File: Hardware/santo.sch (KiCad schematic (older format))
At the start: 7 parts

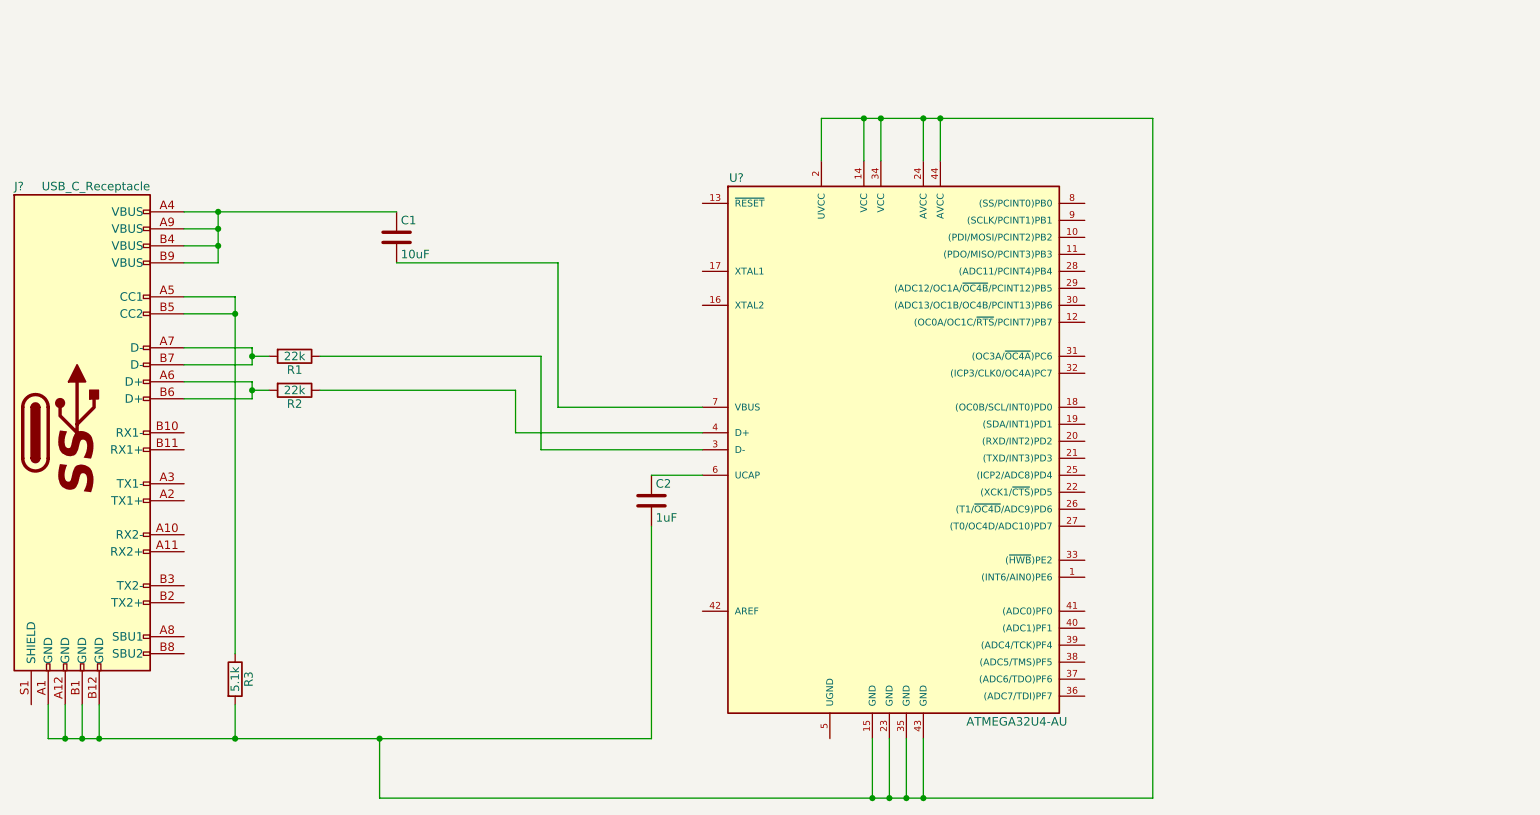
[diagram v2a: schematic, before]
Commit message: Fix title and center
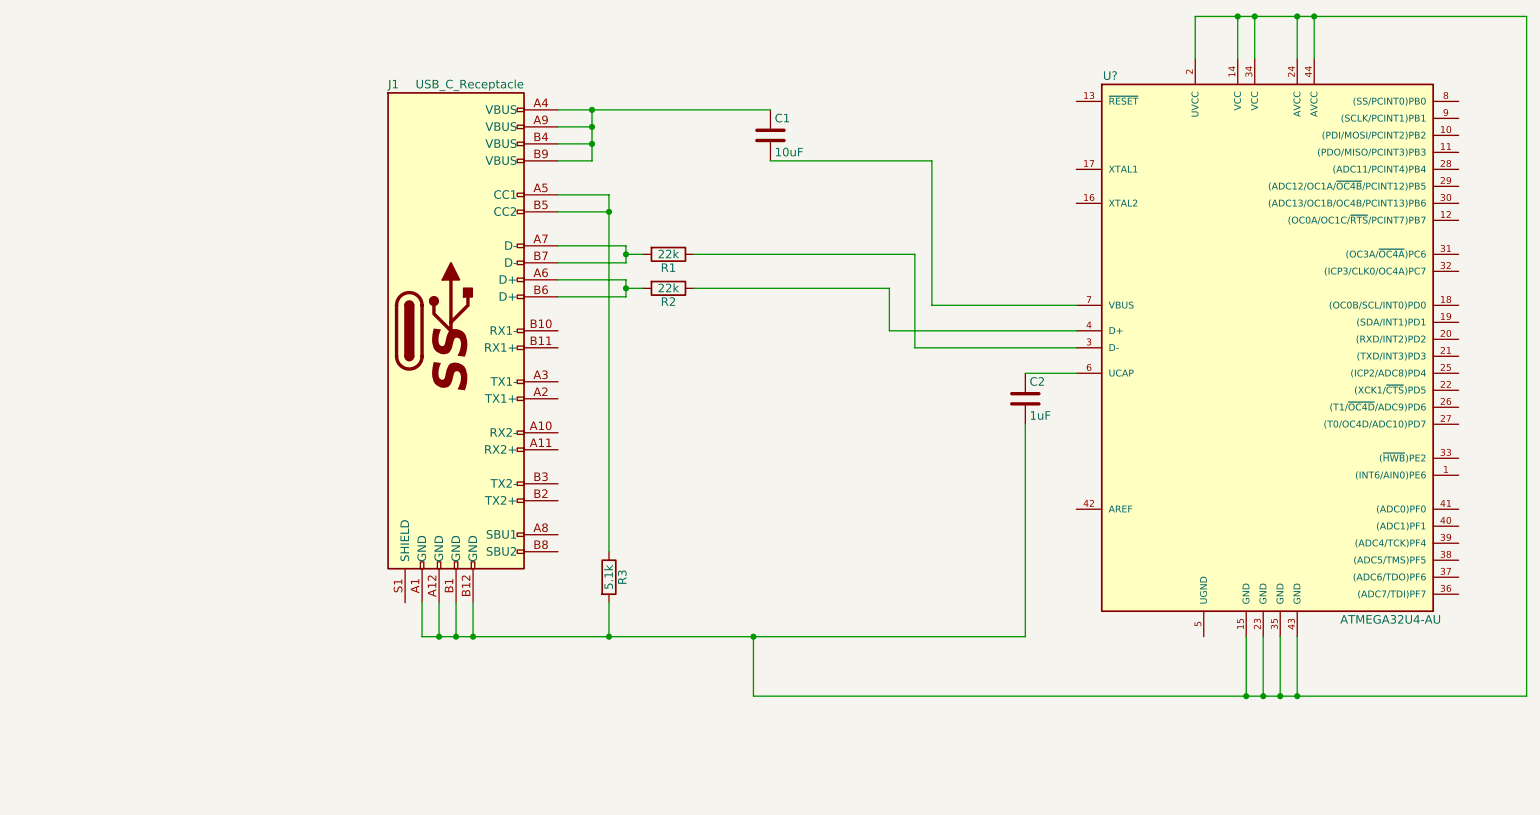
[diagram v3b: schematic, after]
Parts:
- gave numbers to parts that had none: 1
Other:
- moved on the sheet: C1, C2, J1, R1, R2, R3, U?
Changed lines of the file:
@@
 encoding utf-8
 Sheet 1 1
-Title "Controller and Board"
+Title "USB-C Receptacle to Microcontroller"
 Date "2017-10-27"
 Rev "0"
@@
 L ATMEGA32U4-AU U?
 U 1 1 59F3E9EC
-P 5800 4350
-F 0 "U?" H 4850 6050 50  0000 C CNN
-F 1 "ATMEGA32U4-AU" H 6500 2850 50  0000 C CNN
-F 2 "TQFP44" H 5800 4350 50  0001 C CIN
-F 3 "" H 6900 5450 50  0001 C CNN
-	1    5800 4350
-	1    0    0    -1
-$EndComp
-$Comp
-L USB_C_Receptacle J?
+P 8000 3750
+F 0 "U?" H 7050 5450 50  0000 C CNN
+F 1 "ATMEGA32U4-AU" H 8700 2250 50  0000 C CNN
+F 2 "TQFP44" H 8000 3750 50  0001 C CIN
+F 3 "" H 9100 4850 50  0001 C CNN
+	1    8000 3750
+	1    0    0    -1
+$EndComp
+$Comp
+L USB_C_Receptacle J1
 U 1 1 59F5288B
-P 1000 4150
-F 0 "J?" H 600 5600 50  0000 L CNN
-F 1 "USB_C_Receptacle" H 1400 5600 50  0000 R CNN
-F 2 "" H 1150 4150 50  0001 C CNN
-F 3 "" H 1150 4150 50  0001 C CNN
-	1    1000 4150
-	1    0    0    -1
-$EndComp
-Wire Wire Line
-	1600 2950 1800 2950
-Wire Wire Line
-	1800 2850 1800 3150
-Connection ~ 1800 2850
-Wire Wire Line
-	1800 3050 1600 3050
-Connection ~ 1800 2950
-Wire Wire Line
-	1800 3150 1600 3150
-Connection ~ 1800 3050
-Wire Wire Line
-	1600 2850 2850 2850
+P 3200 3550
+F 0 "J1" H 2800 5000 50  0000 L CNN
+F 1 "USB_C_Receptacle" H 3600 5000 50  0000 R CNN
+F 2 "" H 3350 3550 50  0001 C CNN
+F 3 "" H 3350 3550 50  0001 C CNN
+	1    3200 3550
+	1    0    0    -1
+$EndComp
+Wire Wire Line
+	3800 2350 4000 2350
+Wire Wire Line
+	4000 2250 4000 2550
+Connection ~ 4000 2250
+Wire Wire Line
+	4000 2450 3800 2450
+Connection ~ 4000 2350
+Wire Wire Line
+	4000 2550 3800 2550
+Connection ~ 4000 2450
+Wire Wire Line
+	3800 2250 5050 2250
 $Comp
 L C C1
 U 1 1 59F5311D
-P 2850 3000
-F 0 "C1" H 2875 3100 50  0000 L CNN
-F 1 "10uF" H 2875 2900 50  0000 L CNN
-F 2 "" H 2888 2850 50  0001 C CNN
-F 3 "" H 2850 3000 50  0001 C CNN
-	1    2850 3000
-	1    0    0    -1
-$EndComp
-Wire Wire Line
-	2850 3150 3800 3150
-Wire Wire Line
-	3800 3150 3800 4000
-Wire Wire Line
-	3800 4000 4650 4000
+P 5050 2400
+F 0 "C1" H 5075 2500 50  0000 L CNN
+F 1 "10uF" H 5075 2300 50  0000 L CNN
+F 2 "" H 5088 2250 50  0001 C CNN
+F 3 "" H 5050 2400 50  0001 C CNN
+	1    5050 2400
+	1    0    0    -1
+$EndComp
+Wire Wire Line
+	5050 2550 6000 2550
+Wire Wire Line
+	6000 2550 6000 3400
+Wire Wire Line
+	6000 3400 6850 3400
 $Comp
 L C C2
 U 1 1 59F532C4
-P 4350 4550
-F 0 "C2" H 4375 4650 50  0000 L CNN
-F 1 "1uF" H 4375 4450 50  0000 L CNN
-F 2 "" H 4388 4400 50  0001 C CNN
-F 3 "" H 4350 4550 50  0001 C CNN
-	1    4350 4550
-	1    0    0    -1
-$EndComp
-Wire Wire Line
-	4350 4400 4650 4400
-Wire Wire Line
-	4350 4700 4350 5950
-Wire Wire Line
-	4350 5950 800  5950
-Wire Wire Line
-	800  5950 800  5750
-Wire Wire Line
-	900  5750 900  5950
-Connection ~ 900  5950
-Wire Wire Line
-	1000 5750 1000 5950
-Connection ~ 1000 5950
-Wire Wire Line
-	1100 5750 1100 5950
-Connection ~ 1100 5950
-Wire Wire Line
-	5350 2550 5350 2300
-Wire Wire Line
-	5350 2300 7300 2300
-Wire Wire Line
-	7300 2300 7300 6300
-Wire Wire Line
-	7300 6300 2750 6300
-Wire Wire Line
-	2750 6300 2750 5950
-Connection ~ 2750 5950
-Wire Wire Line
-	5600 2550 5600 2300
-Connection ~ 5600 2300
-Wire Wire Line
-	5700 2550 5700 2300
-Connection ~ 5700 2300
-Wire Wire Line
-	5950 2550 5950 2300
-Connection ~ 5950 2300
-Wire Wire Line
-	6050 2550 6050 2300
-Connection ~ 6050 2300
-Wire Wire Line
-	5650 5950 5650 6300
-Connection ~ 5650 6300
-Wire Wire Line
-	5750 5950 5750 6300
-Connection ~ 5750 6300
-Wire Wire Line
-	5850 5950 5850 6300
-Connection ~ 5850 6300
-Wire Wire Line
-	5950 5950 5950 6300
-Connection ~ 5950 6300
+P 6550 3950
+F 0 "C2" H 6575 4050 50  0000 L CNN
+F 1 "1uF" H 6575 3850 50  0000 L CNN
+F 2 "" H 6588 3800 50  0001 C CNN
+F 3 "" H 6550 3950 50  0001 C CNN
+	1    6550 3950
+	1    0    0    -1
+$EndComp
+Wire Wire Line
+	6550 3800 6850 3800
+Wire Wire Line
+	6550 4100 6550 5350
+Wire Wire Line
+	6550 5350 3000 5350
+Wire Wire Line
+	3000 5350 3000 5150
+Wire Wire Line
+	3100 5150 3100 5350
+Connection ~ 3100 5350
+Wire Wire Line
+	3200 5150 3200 5350
+Connection ~ 3200 5350
+Wire Wire Line
+	3300 5150 3300 5350
+Connection ~ 3300 5350
+Wire Wire Line
+	7550 1950 7550 1700
+Wire Wire Line
+	7550 1700 9500 1700
+Wire Wire Line
+	9500 1700 9500 5700
+Wire Wire Line
+	9500 5700 4950 5700
+Wire Wire Line
+	4950 5700 4950 5350
+Connection ~ 4950 5350
+Wire Wire Line
+	7800 1950 7800 1700
+Connection ~ 7800 1700
+Wire Wire Line
+	7900 1950 7900 1700
+Connection ~ 7900 1700
+Wire Wire Line
+	8150 1950 8150 1700
+Connection ~ 8150 1700
+Wire Wire Line
+	8250 1950 8250 1700
+Connection ~ 8250 1700
+Wire Wire Line
+	7850 5350 7850 5700
+Connection ~ 7850 5700
+Wire Wire Line
+	7950 5350 7950 5700
+Connection ~ 7950 5700
+Wire Wire Line
+	8050 5350 8050 5700
+Connection ~ 8050 5700
+Wire Wire Line
+	8150 5350 8150 5700
+Connection ~ 8150 5700
 $Comp
 L R R3
 U 1 1 59F605C4
-P 1900 5600
-F 0 "R3" V 1980 5600 50  0000 C CNN
-F 1 "5.1k" V 1900 5600 50  0000 C CNN
-F 2 "" V 1830 5600 50  0001 C CNN
-F 3 "" H 1900 5600 50  0001 C CNN
-	1    1900 5600
-	1    0    0    -1
-$EndComp
-Wire Wire Line
-	1600 3350 1900 3350
-Wire Wire Line
-	1900 3350 1900 5450
-Wire Wire Line
-	1600 3450 1900 3450
-Connection ~ 1900 3450
-Wire Wire Line
-	1900 5750 1900 5950
-Connection ~ 1900 5950
+P 4100 5000
+F 0 "R3" V 4180 5000 50  0000 C CNN
+F 1 "5.1k" V 4100 5000 50  0000 C CNN
+F 2 "" V 4030 5000 50  0001 C CNN
+F 3 "" H 4100 5000 50  0001 C CNN
+	1    4100 5000
+	1    0    0    -1
+$EndComp
+Wire Wire Line
+	3800 2750 4100 2750
+Wire Wire Line
+	4100 2750 4100 4850
+Wire Wire Line
+	3800 2850 4100 2850
+Connection ~ 4100 2850
+Wire Wire Line
+	4100 5150 4100 5350
+Connection ~ 4100 5350
 $Comp
 L R R1
 U 1 1 59F60892
-P 2250 3700
-F 0 "R1" V 2330 3700 50  0000 C CNN
-F 1 "22k" V 2250 3700 50  0000 C CNN
-F 2 "" V 2180 3700 50  0001 C CNN
-F 3 "" H 2250 3700 50  0001 C CNN
-	1    2250 3700
+P 4450 3100
+F 0 "R1" V 4530 3100 50  0000 C CNN
+F 1 "22k" V 4450 3100 50  0000 C CNN
+F 2 "" V 4380 3100 50  0001 C CNN
+F 3 "" H 4450 3100 50  0001 C CNN
+	1    4450 3100
 	0    1    1    0
 $EndComp
@@
 L R R2
 U 1 1 59F608F2
-P 2250 3900
-F 0 "R2" V 2330 3900 50  0000 C CNN
-F 1 "22k" V 2250 3900 50  0000 C CNN
-F 2 "" V 2180 3900 50  0001 C CNN
-F 3 "" H 2250 3900 50  0001 C CNN
-	1    2250 3900
+P 4450 3300
+F 0 "R2" V 4530 3300 50  0000 C CNN
+F 1 "22k" V 4450 3300 50  0000 C CNN
+F 2 "" V 4380 3300 50  0001 C CNN
+F 3 "" H 4450 3300 50  0001 C CNN
+	1    4450 3300
 	0    1    1    0
 $EndComp
 Wire Wire Line
-	1600 3650 2000 3650
-Wire Wire Line
-	2000 3650 2000 3750
-Wire Wire Line
-	2000 3700 2100 3700
-Wire Wire Line
-	2000 3750 1600 3750
-Connection ~ 2000 3700
-Wire Wire Line
-	2000 3950 1600 3950
-Wire Wire Line
-	2000 3850 2000 3950
-Wire Wire Line
-	2000 3900 2100 3900
-Wire Wire Line
-	1600 3850 2000 3850
-Connection ~ 2000 3900
-Wire Wire Line
-	2400 3700 3700 3700
-Wire Wire Line
-	3700 3700 3700 4250
-Wire Wire Line
-	3700 4250 4650 4250
-Wire Wire Line
-	2400 3900 3550 3900
-Wire Wire Line
-	3550 3900 3550 4150
-Wire Wire Line
-	3550 4150 4650 4150
+	3800 3050 4200 3050
+Wire Wire Line
+	4200 3050 4200 3150
+Wire Wire Line
+	4200 3100 4300 3100
+Wire Wire Line
+	4200 3150 3800 3150
+Connection ~ 4200 3100
+Wire Wire Line
+	4200 3350 3800 3350
+Wire Wire Line
+	4200 3250 4200 3350
+Wire Wire Line
+	4200 3300 4300 3300
+Wire Wire Line
+	3800 3250 4200 3250
+Connection ~ 4200 3300
+Wire Wire Line
+	4600 3100 5900 3100
+Wire Wire Line
+	5900 3100 5900 3650
+Wire Wire Line
+	5900 3650 6850 3650
+Wire Wire Line
+	4600 3300 5750 3300
+Wire Wire Line
+	5750 3300 5750 3550
+Wire Wire Line
+	5750 3550 6850 3550
 $EndSCHEMATC

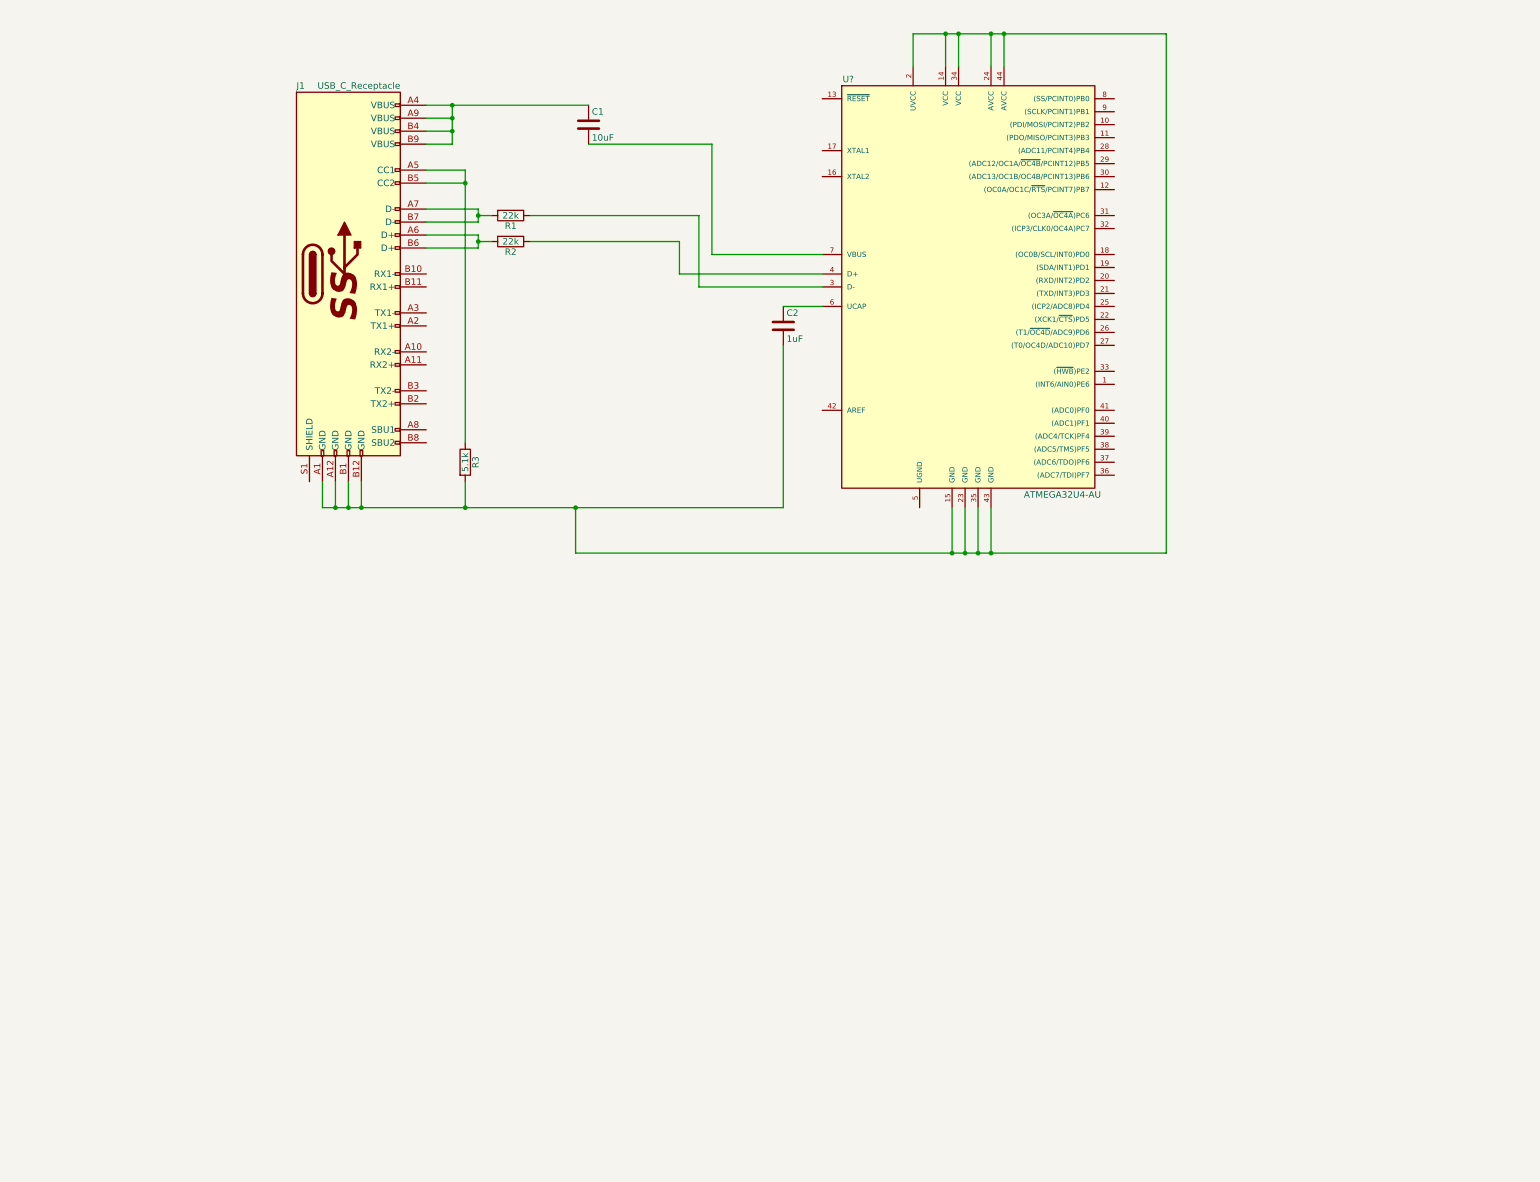
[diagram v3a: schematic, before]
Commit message: Fix the wiring for USB-C & Add TRRS Jack
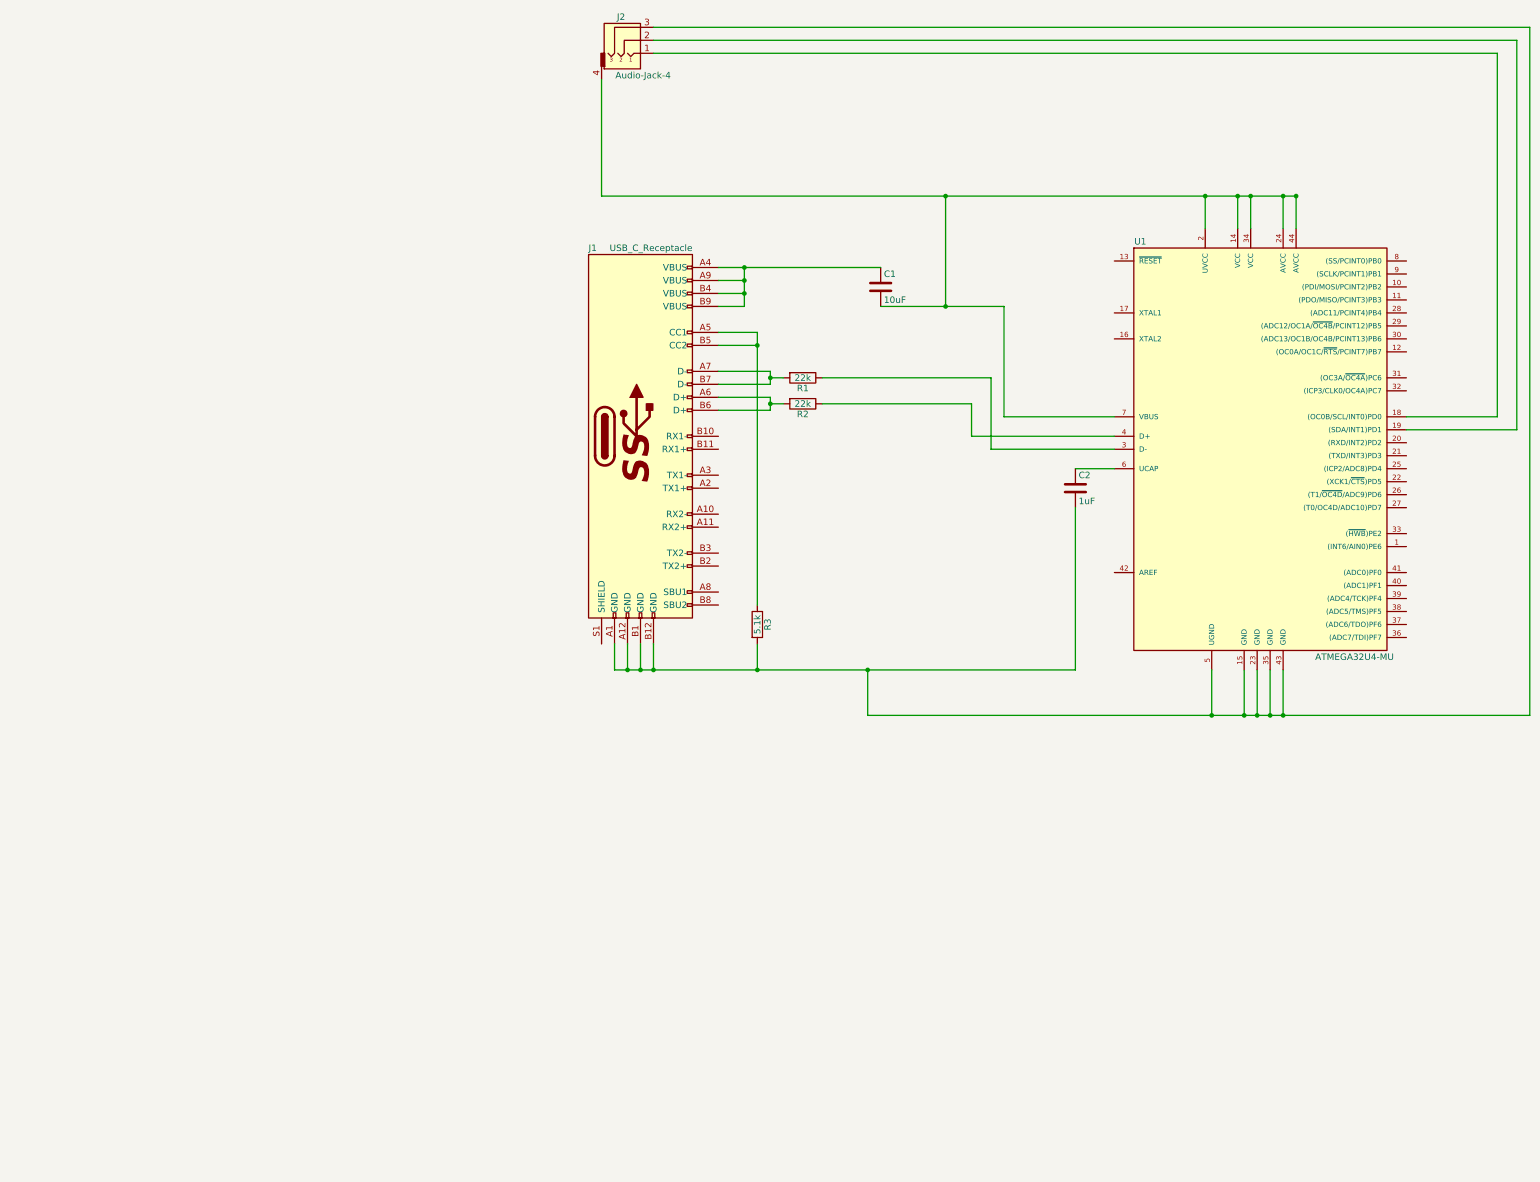
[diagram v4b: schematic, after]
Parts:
- removed U?: ATMEGA32U4-AU, TQFP44, symbol ATMEGA32U4-AU
- added J2: Audio-Jack-4, symbol Audio-Jack-4
- added U1: ATMEGA32U4-MU, QFN44, symbol ATMEGA32U4-MU
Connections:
- net at C2.2, J1.A1 (GND), J1.A12 (GND)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: now also J2.3, U1.15 (GND), U1.23 (GND), U1.35 (GND), U1.43 (GND), U1.5 (UGND)
- net at R1.1: now also U1.3 (D-)
- net at R2.1: now also U1.4 (D+)
- net at C2.1: now also U1.6 (UCAP)
- net at C1.2: now also J2.4, U1.14 (VCC), U1.2 (UVCC), U1.24 (AVCC), U1.34 (VCC), U1.44 (AVCC), U1.7 (VBUS)
- new net: J2.1, U1.18 ((OC0B/SCL/INT0)PD0)
- new net: J2.2, U1.19 ((SDA/INT1)PD1)
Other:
- moved on the sheet: C1, C2, J1, R1, R2, R3
